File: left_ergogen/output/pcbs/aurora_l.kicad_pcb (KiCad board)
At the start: 2 copper layers, 118 x 114.2 mm, 89 parts

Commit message: Refine left board further
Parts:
- removed the REF** at (100.0, 104.0)
- removed the REF** at (136.0, 87.0)
- removed the REF** at (136.0, 70.0)
- removed the REF** at (136.0, 53.0)
- removed the REF** at (154.0, 104.0)
- removed the REF** at (154.0, 87.0)
- removed the REF** at (154.0, 70.0)
- removed the REF** at (154.0, 53.0)
- removed the REF** at (172.0, 104.0)
- removed the REF** at (172.0, 87.0)
- removed the REF** at (172.0, 70.0)
- removed the REF** at (100.0, 87.0)
- removed the REF** at (172.0, 53.0)
- removed the REF** at (190.0, 104.0)
- removed the REF** at (190.0, 87.0)
- removed the REF** at (190.0, 70.0)
- removed the REF** at (190.0, 53.0)
- removed the REF** at (102.2, 121.0)
- removed the REF** at (124.8, 121.0)
- removed the REF** at (147.2, 121.0)
- removed the REF** at (178.8, 121.0)
- removed the REF** at (100.0, 70.0)
- removed the REF** at (100.0, 53.0)
- removed the REF** at (118.0, 104.0)
- removed the REF** at (118.0, 87.0)
- removed the REF** at (118.0, 70.0)
- removed the REF** at (118.0, 53.0)
- removed the REF** at (136.0, 104.0)
- added ?: , HOLE_M2_TH, F.Cu at (148.6, 28.6)
- added ?: , HOLE_M2_TH, F.Cu at (184.6, 37.1)
- added ?: , HOLE_M2_TH, F.Cu at (87.8, 122.1)
- added REF**: WS2812, WS2812-2020, F.Cu at (100.0, 88.0)
- added REF**: WS2812, WS2812-2020, F.Cu at (172.0, 54.0)
- added REF**: WS2812, WS2812-2020, F.Cu at (190.0, 88.0)
- added REF**: WS2812, WS2812-2020, F.Cu at (190.0, 54.0)
- added REF**: WS2812, WS2812-2020, F.Cu at (102.2, 122.0)
- added REF**: WS2812, WS2812-2020, F.Cu at (124.8, 122.0)
- added REF**: WS2812, WS2812-2020, F.Cu at (147.2, 122.0)
- added REF**: WS2812, WS2812-2020, F.Cu at (178.8, 122.0)
- added REF**: WS2812, WS2812-2020, F.Cu at (100.0, 105.0)
- added REF**: WS2812, WS2812-2020, F.Cu at (100.0, 71.0)
- added REF**: WS2812, WS2812-2020, F.Cu at (118.0, 105.0)
- added REF**: WS2812, WS2812-2020, F.Cu at (100.0, 54.0)
- added REF**: WS2812, WS2812-2020, F.Cu at (118.0, 71.0)
- added REF**: WS2812, WS2812-2020, F.Cu at (136.0, 105.0)
- added REF**: WS2812, WS2812-2020, F.Cu at (136.0, 71.0)
- added REF**: WS2812, WS2812-2020, F.Cu at (154.0, 105.0)
- added REF**: WS2812, WS2812-2020, F.Cu at (154.0, 71.0)
- added REF**: WS2812, WS2812-2020, F.Cu at (172.0, 105.0)
- added REF**: WS2812, WS2812-2020, F.Cu at (172.0, 71.0)
- added REF**: WS2812, WS2812-2020, F.Cu at (190.0, 105.0)
- added REF**: WS2812, WS2812-2020, F.Cu at (190.0, 71.0)
- added REF**: WS2812, WS2812-2020, F.Cu at (118.0, 88.0)
- added REF**: WS2812, WS2812-2020, F.Cu at (118.0, 54.0)
- added REF**: WS2812, WS2812-2020, F.Cu at (136.0, 88.0)
- added REF**: WS2812, WS2812-2020, F.Cu at (136.0, 54.0)
- added REF**: WS2812, WS2812-2020, F.Cu at (154.0, 88.0)
- added REF**: WS2812, WS2812-2020, F.Cu at (154.0, 54.0)
- added REF**: WS2812, WS2812-2020, F.Cu at (172.0, 88.0)
- moved D1 1.00 mm to (100.0, 108.0)
- moved D10 1.00 mm to (136.0, 91.0)
- moved D11 1.00 mm to (136.0, 74.0)
- moved D12 1.00 mm to (136.0, 57.0)
- moved D13 1.00 mm to (154.0, 108.0)
- moved D14 1.00 mm to (154.0, 91.0)
- moved D15 1.00 mm to (154.0, 74.0)
- moved D16 1.00 mm to (154.0, 57.0)
- moved D17 1.00 mm to (172.0, 108.0)
- moved D18 1.00 mm to (172.0, 91.0)
- moved D19 1.00 mm to (172.0, 74.0)
- moved D2 1.00 mm to (100.0, 91.0)
- moved D20 1.00 mm to (172.0, 57.0)
- moved D21 1.00 mm to (190.0, 108.0)
- moved D22 1.00 mm to (190.0, 91.0)
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
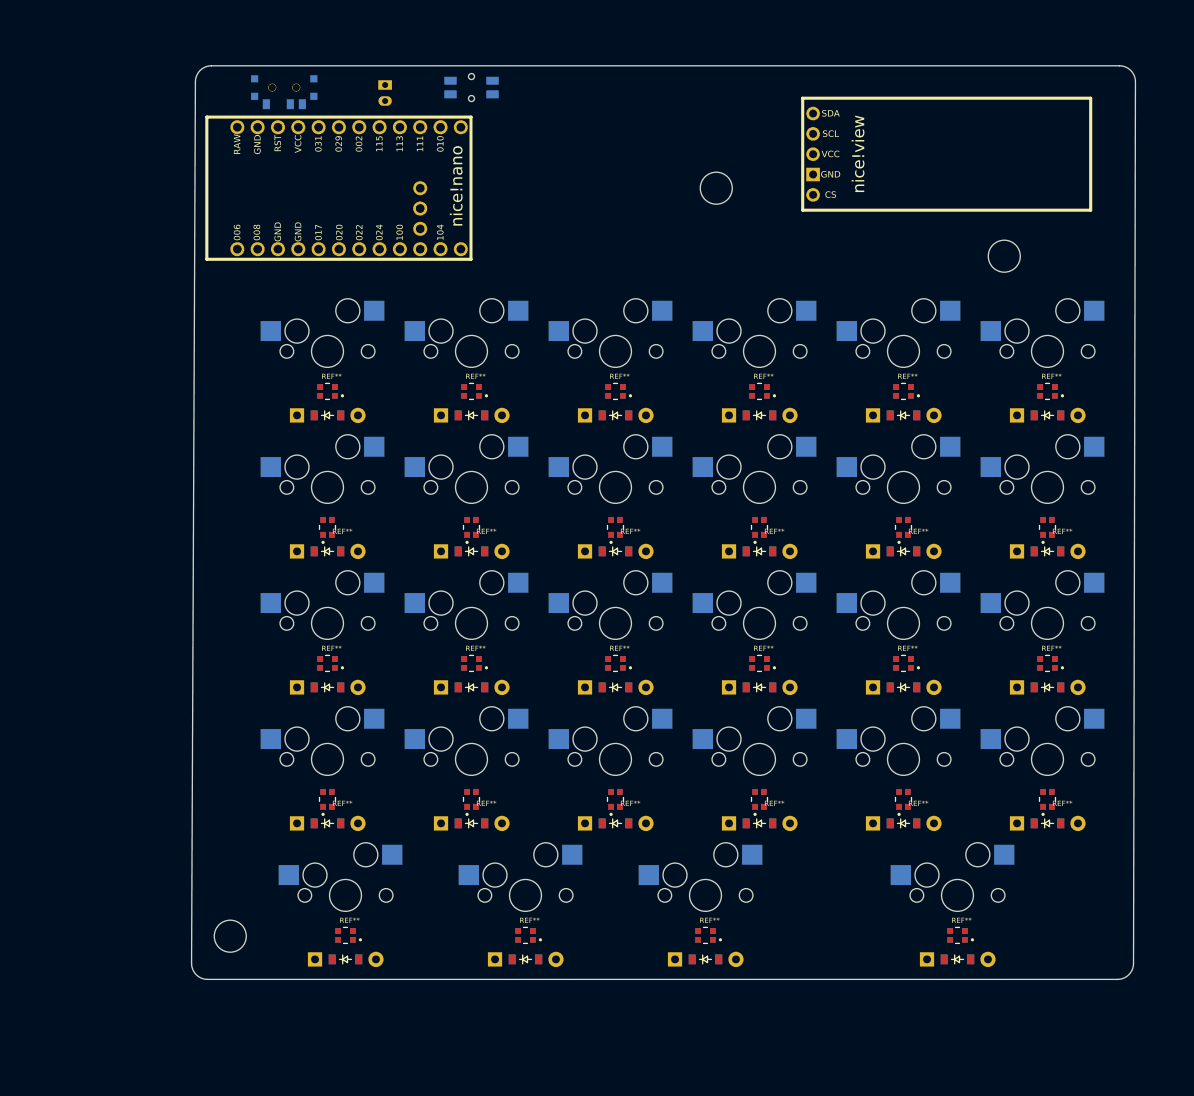
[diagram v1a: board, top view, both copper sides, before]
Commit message: Key clearance fixes and mounting hole placement fixes
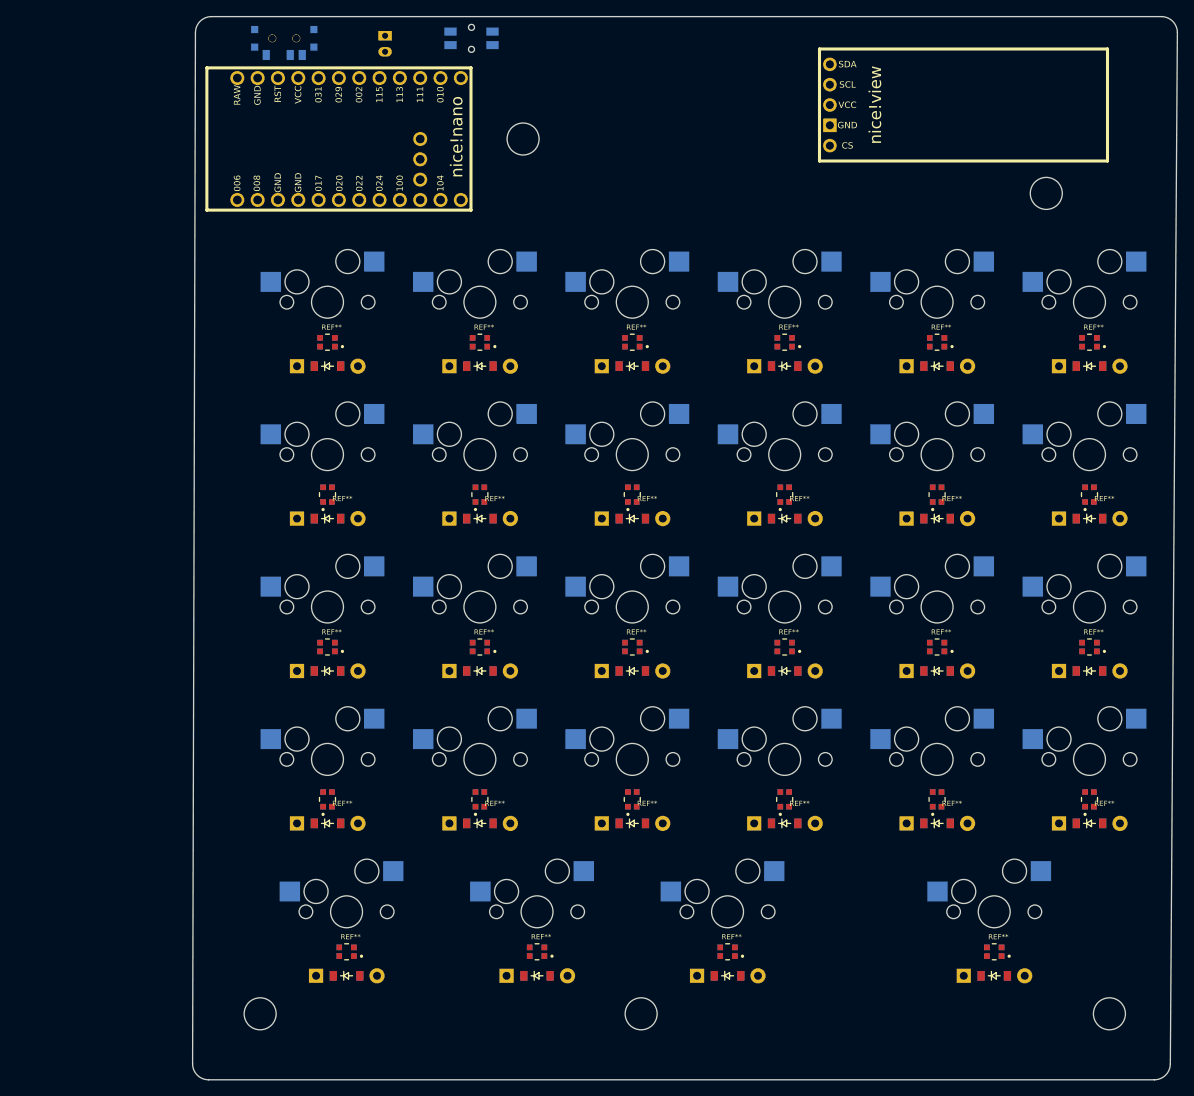
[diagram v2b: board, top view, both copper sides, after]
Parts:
- removed the ? at (148.6, 28.6)
- removed the ? at (184.6, 37.1)
- removed the ? at (87.8, 122.1)
- removed the REF** at (100.0, 88.0)
- removed the REF** at (172.0, 54.0)
- removed the REF** at (190.0, 88.0)
- removed the REF** at (190.0, 54.0)
- removed the REF** at (102.2, 122.0)
- removed the REF** at (124.8, 122.0)
- removed the REF** at (147.2, 122.0)
- removed the REF** at (178.8, 122.0)
- removed the REF** at (100.0, 71.0)
- removed the REF** at (118.0, 105.0)
- removed the REF** at (100.0, 54.0)
- removed the REF** at (118.0, 71.0)
- removed the REF** at (136.0, 105.0)
- removed the REF** at (136.0, 71.0)
- removed the REF** at (154.0, 105.0)
- removed the REF** at (154.0, 71.0)
- removed the REF** at (172.0, 105.0)
- removed the REF** at (172.0, 71.0)
- removed the REF** at (190.0, 105.0)
- removed the REF** at (190.0, 71.0)
- removed the REF** at (118.0, 88.0)
- removed the REF** at (118.0, 54.0)
- removed the REF** at (136.0, 88.0)
- removed the REF** at (136.0, 54.0)
- removed the REF** at (154.0, 88.0)
- removed the REF** at (154.0, 54.0)
- removed the REF** at (172.0, 88.0)
- added ?: , HOLE_M2_TH, F.Cu at (124.5, 22.5)
- added ?: , HOLE_M2_TH, F.Cu at (189.8, 29.3)
- added ?: , HOLE_M2_TH, F.Cu at (91.6, 131.8)
- added ?: , HOLE_M2_TH, F.Cu at (139.2, 131.8)
- added ?: , HOLE_M2_TH, F.Cu at (197.7, 131.8)
- added REF**: WS2812, WS2812-2020, F.Cu at (100.0, 86.0)
- added REF**: WS2812, WS2812-2020, F.Cu at (176.2, 47.9)
- added REF**: WS2812, WS2812-2020, F.Cu at (195.2, 86.0)
- added REF**: WS2812, WS2812-2020, F.Cu at (195.2, 47.9)
- added REF**: WS2812, WS2812-2020, F.Cu at (102.4, 124.0)
- added REF**: WS2812, WS2812-2020, F.Cu at (126.2, 124.0)
- added REF**: WS2812, WS2812-2020, F.Cu at (150.0, 124.0)
- added REF**: WS2812, WS2812-2020, F.Cu at (183.3, 124.0)
- added REF**: WS2812, WS2812-2020, F.Cu at (100.0, 66.9)
- added REF**: WS2812, WS2812-2020, F.Cu at (119.0, 105.0)
- added REF**: WS2812, WS2812-2020, F.Cu at (100.0, 47.9)
- added REF**: WS2812, WS2812-2020, F.Cu at (119.0, 66.9)
- added REF**: WS2812, WS2812-2020, F.Cu at (138.1, 105.0)
- added REF**: WS2812, WS2812-2020, F.Cu at (138.1, 66.9)
- added REF**: WS2812, WS2812-2020, F.Cu at (157.2, 105.0)
- added REF**: WS2812, WS2812-2020, F.Cu at (157.2, 66.9)
- added REF**: WS2812, WS2812-2020, F.Cu at (176.2, 105.0)
- added REF**: WS2812, WS2812-2020, F.Cu at (176.2, 66.9)
- added REF**: WS2812, WS2812-2020, F.Cu at (195.2, 105.0)
- added REF**: WS2812, WS2812-2020, F.Cu at (195.2, 66.9)
- added REF**: WS2812, WS2812-2020, F.Cu at (119.0, 86.0)
- added REF**: WS2812, WS2812-2020, F.Cu at (119.0, 47.9)
- added REF**: WS2812, WS2812-2020, F.Cu at (138.1, 86.0)
- added REF**: WS2812, WS2812-2020, F.Cu at (138.1, 47.9)
- added REF**: WS2812, WS2812-2020, F.Cu at (157.2, 86.0)
- added REF**: WS2812, WS2812-2020, F.Cu at (157.2, 47.9)
- added REF**: WS2812, WS2812-2020, F.Cu at (176.2, 86.0)
- moved D24 8.09 mm to (195.2, 50.9)
- moved S24 8.09 mm to (195.2, 42.9)
- moved D20 7.45 mm to (176.2, 50.9)
- moved S20 7.45 mm to (176.2, 42.9)
- moved D16 6.91 mm to (157.2, 50.9)
- moved S16 6.91 mm to (157.2, 42.9)
- moved D23 6.66 mm to (195.2, 69.9)
- moved S23 6.66 mm to (195.2, 61.9)
- moved D12 6.50 mm to (138.1, 50.9)
- moved S12 6.50 mm to (138.1, 42.9)
- moved niceView1 6.50 mm to (161.5, 18.2)
- moved D8 6.24 mm to (119.0, 50.9)
- moved S8 6.24 mm to (119.0, 42.9)
- moved B1 6.15 mm to (118.0, 9.87)
- moved D4 6.15 mm to (100.0, 50.9)
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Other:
- board size 118 x 114.2 mm -> 123.1 x 132.9 mm

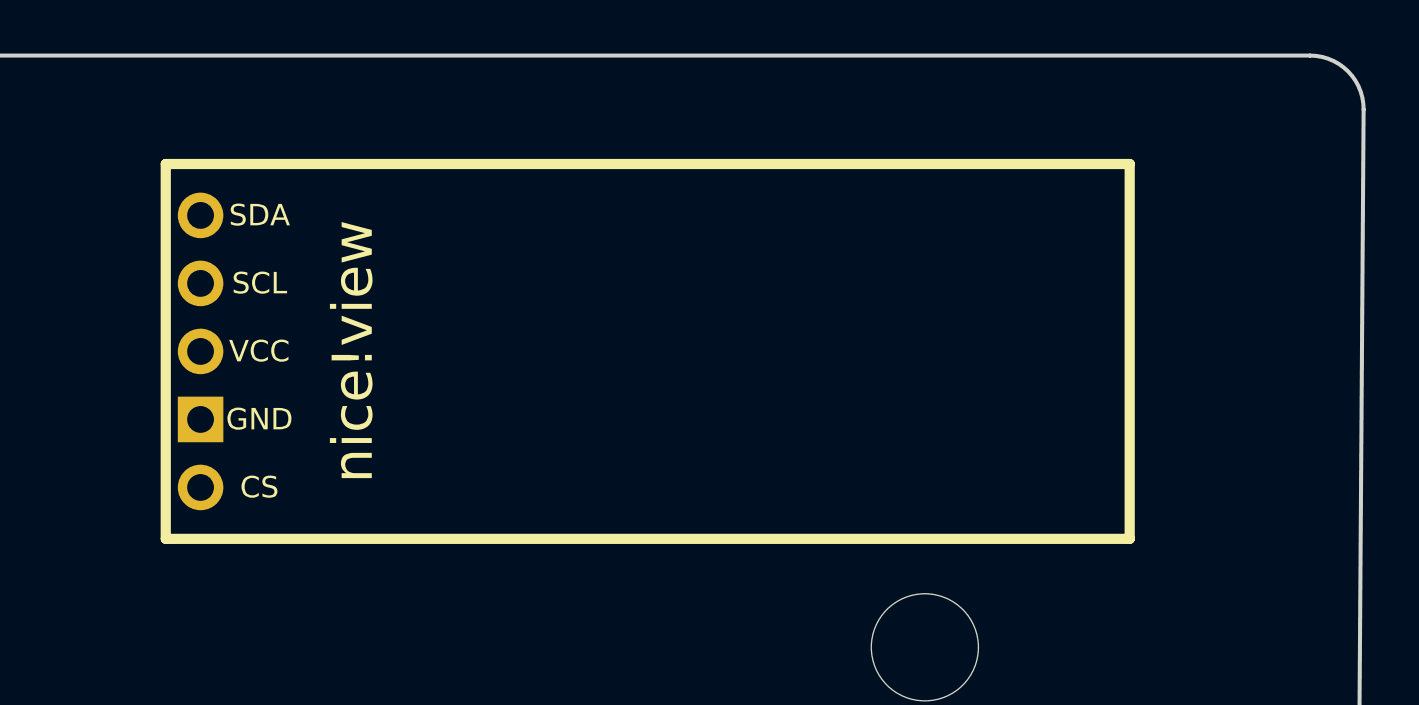
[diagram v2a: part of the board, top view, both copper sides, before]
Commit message: Left PCB dimensioning tweaks
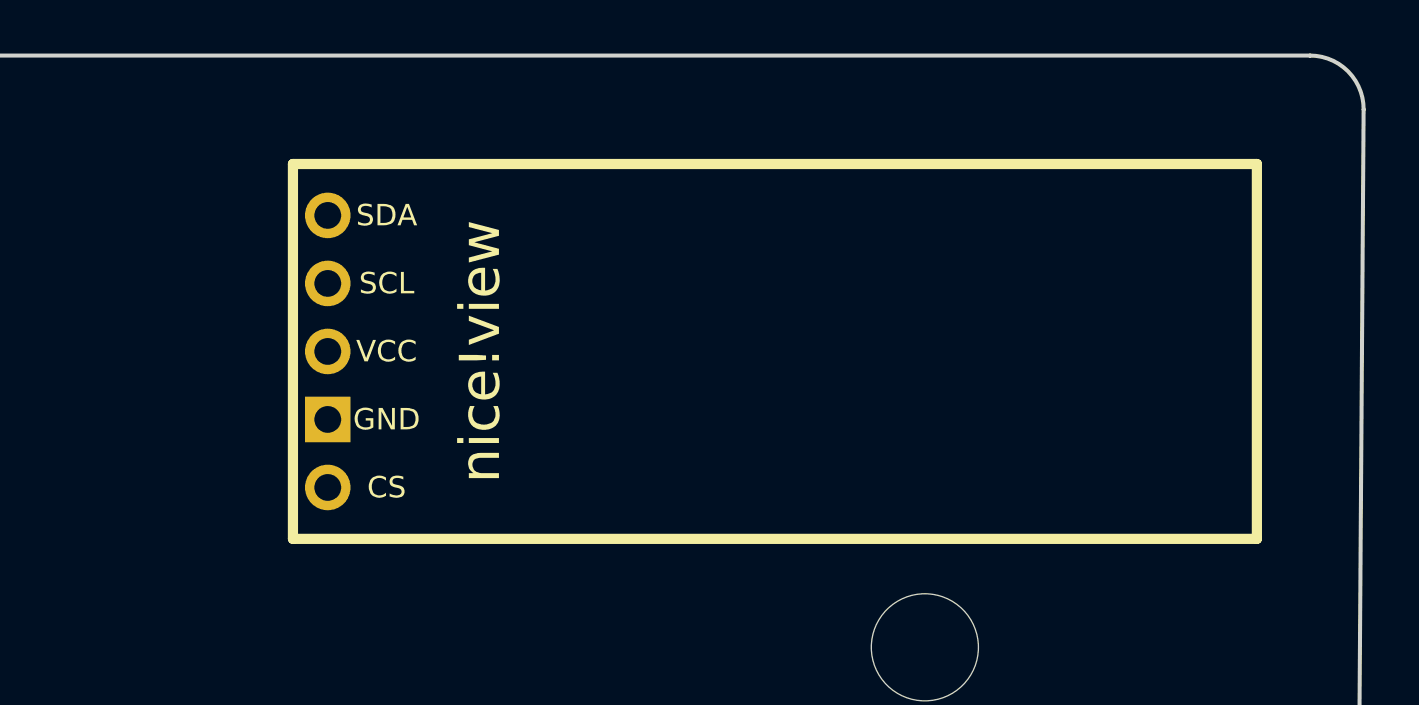
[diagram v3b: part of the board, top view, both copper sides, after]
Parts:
- moved niceView1 4.75 mm to (166.2, 18.2)
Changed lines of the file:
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@@
         )
         (module lib:niceView_headers (layer F.Cu)
-        (at 161.5 18.20000000000001 0)
+        (at 166.25 18.20000000000001 0)
         (fp_text reference "niceView1" (at 0 0) (layer F.SilkS) hide (effects (font (size 1.27 1.27) (thickness 0.15))))
         (fp_text value niceView (at -1.3 0) (layer F.Fab) hide (effects (font (size 1 1) (thickness 0.15))))

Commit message: Redesign left PCB board layout
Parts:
- removed the ? at (124.5, 22.5)
- removed the ? at (189.8, 29.3)
- removed the ? at (91.6, 131.8)
- removed the ? at (139.2, 131.8)
- removed the ? at (197.7, 131.8)
- added ?: , HOLE_M2_TH, F.Cu at (109.5, 52.4)
- added ?: , HOLE_M2_TH, F.Cu at (185.7, 52.4)
- added ?: , HOLE_M2_TH, F.Cu at (109.5, 90.5)
- added ?: , HOLE_M2_TH, F.Cu at (185.7, 90.5)
- moved niceView1 117.7 mm to (73.3, 90.5), turned to -90 degrees
- moved T1 86.4 mm to (63.4, 90.5), turned to 90 degrees
- moved B1 78.8 mm to (63.4, 66.7), turned to 90 degrees
- moved JST1 77.7 mm to (65.7, 76.2), turned to 0 degrees
- moved MCU1 36.0 mm to (75.2, 45.7), turned to -90 degrees
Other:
- board size 123.1 x 132.9 mm -> 145.1 x 107.7 mm

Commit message: Left PCB pin layout fixes and full routed pcb
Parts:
- moved D25 2.00 mm to (102.4, 129.1)
- moved D26 2.00 mm to (126.2, 129.1)
- moved D27 2.00 mm to (150.0, 129.1)
- moved D28 2.00 mm to (183.3, 129.1)
- moved D1 2.00 mm to (100.0, 110.0)
- moved D10 2.00 mm to (138.1, 91.0)
- moved D11 2.00 mm to (138.1, 71.9)
- moved D12 2.00 mm to (138.1, 52.9)
- moved D13 2.00 mm to (157.2, 110.0)
- moved D14 2.00 mm to (157.2, 91.0)
- moved D15 2.00 mm to (157.2, 71.9)
- moved D16 2.00 mm to (157.2, 52.9)
- moved D17 2.00 mm to (176.2, 110.0)
- moved D18 2.00 mm to (176.2, 91.0)
- moved D19 2.00 mm to (176.2, 71.9)
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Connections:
- D1 pad 1: P113 -> P115
- D10 pad 1: P115 -> P002
- D11 pad 1: P002 -> P029
- D12 pad 1: P029 -> P031
- D13 pad 1: P113 -> P115
- D14 pad 1: P115 -> P002
- D15 pad 1: P002 -> P029
- D16 pad 1: P029 -> P031
- D17 pad 1: P113 -> P115
- D18 pad 1: P115 -> P002
- D19 pad 1: P002 -> P029
- D2 pad 1: P115 -> P002
- D20 pad 1: P029 -> P031
- D21 pad 1: P113 -> P115
- D22 pad 1: P115 -> P002
- D23 pad 1: P002 -> P029
- D24 pad 1: P029 -> P031
- D25 pad 1: P031 -> P113
- D26 pad 1: P031 -> P113
- D27 pad 1: P031 -> P113
- D28 pad 1: P031 -> P113
- D3 pad 1: P002 -> P029
- D4 pad 1: P029 -> P031
- D5 pad 1: P113 -> P115
- D6 pad 1: P115 -> P002
- D7 pad 1: P002 -> P029
- D8 pad 1: P029 -> P031
- D9 pad 1: P113 -> P115
- REF** pad 2: P8 -> P010 (x28)
- REF** pad 4: P15 -> P009 (x28)
- S1 pad 2: P020 -> P011
- S13 pad 2: P100 -> P022
- S14 pad 2: P100 -> P022
- S15 pad 2: P100 -> P022
- S16 pad 2: P100 -> P022
- S17 pad 2: P011 -> P020
- S18 pad 2: P011 -> P020
- S19 pad 2: P011 -> P020
- S2 pad 2: P020 -> P011
- S20 pad 2: P011 -> P020
- S25 pad 2: P020 -> P011
- S26 pad 2: P022 -> P100
- S27 pad 2: P024 -> P022
- S28 pad 2: P011 -> P017
- S3 pad 2: P020 -> P011
- S4 pad 2: P020 -> P011
- S5 pad 2: P022 -> P100
- S6 pad 2: P022 -> P100
- S7 pad 2: P022 -> P100
- S8 pad 2: P022 -> P100
- niceView1 pad 1: P006 -> P101
- niceView1 pad 4: P020 -> P102
- niceView1 pad 5: P017 -> P107
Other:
- outline, holes or cut-outs redrawn
